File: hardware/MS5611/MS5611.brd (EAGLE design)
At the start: 15 x 16 mm, 4 parts, among them U1 MS5611, U2 EM406FLAT

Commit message: MS5611
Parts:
- C2: value 100nF -> 0.1uF
- moved R1 6.38 mm to (10.8, 9.47), turned to 270 degrees
- moved U1 0.46 mm to (7.57, 10.4)
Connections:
- removed net N$6: U1.4, U2.5
- new net N$3: U1.5
- new net VCC: U2.1
- net CSB: now also U1.4, U2.5; no longer U1.5
- net N$1: now also C2.1, U1.1; no longer R1.1, U2.2
- net N$2: now also R1.1, U1.6; no longer C2.1, U1.1, U2.1
- net SDO: now also U2.2; no longer U1.6
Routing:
- net N$2: track 11.5 -> 2.34 mm
- net SDO: track 15.1 -> 7.38 mm, vias 0 -> 2
- net CSB: track 0.00 -> 5.05 mm
- net N$6: track 4.81 -> 0.00 mm
- net SDI: track 12.8 -> 16.5 mm
- net SCK: track 16.1 -> 19.5 mm
- net GND: track 10.3 -> 8.08 mm, vias 1 -> 2
- removed copper zone on layer 1, net GND
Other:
- board size 15 x 16 mm -> 14.6 x 14.6 mm
- board text added: "ICARUS SENSORS MS5611 SPI board revA"
- board text removed: "ICARUS SENSORS MS5803 SPI board revA"

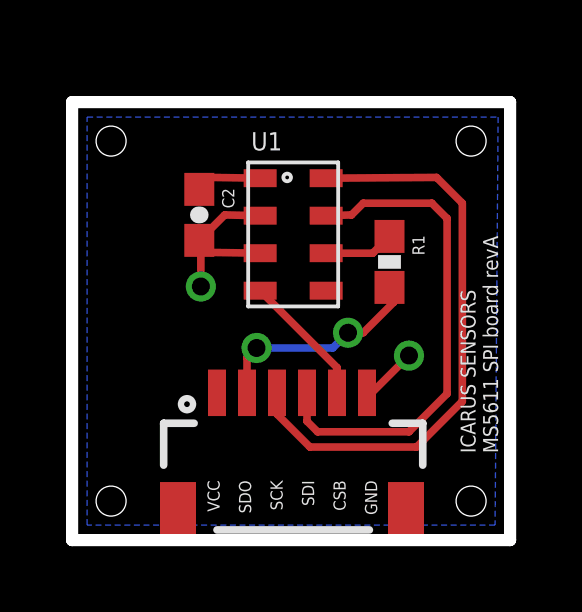
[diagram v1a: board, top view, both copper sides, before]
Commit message: borderless
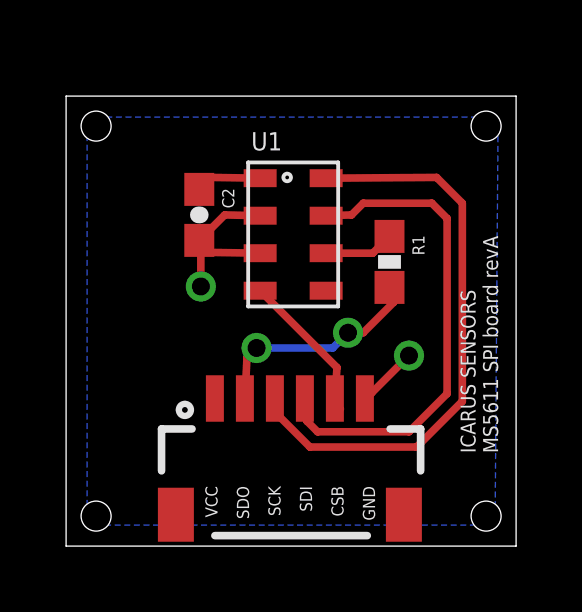
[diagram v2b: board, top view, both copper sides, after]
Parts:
- moved U2 0.20 mm to (7.50, 2.00)
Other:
- board size 14.6 x 14.6 mm -> 15 x 15 mm
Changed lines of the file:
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@@
 <setting verticaltext="up"/>
 </settings>
-<grid distance="0.01" unitdist="inch" unit="inch" style="lines" multiple="1" display="yes" altdistance="0.001" altunitdist="inch" altunit="inch"/>
+<grid distance="1" unitdist="mm" unit="mm" style="lines" multiple="1" display="yes" altdistance="0.001" altunitdist="inch" altunit="inch"/>
 <layers>
 <layer number="1" name="Top" color="4" fill="1" visible="yes" active="yes"/>
@@
 <board>
 <plain>
-<wire x1="0.2" y1="0.2" x2="0.2" y2="14.8" width="0.4064" layer="20"/>
-<wire x1="0.2" y1="14.8" x2="14.8" y2="14.8" width="0.4064" layer="20"/>
-<wire x1="14.8" y1="14.8" x2="14.8" y2="0.2" width="0.4064" layer="20"/>
-<wire x1="14.8" y1="0.2" x2="0.2" y2="0.2" width="0.4064" layer="20"/>
-<hole x="1.5" y="13.5" drill="1"/>
-<hole x="13.5" y="13.5" drill="1"/>
-<hole x="13.5" y="1.5" drill="1"/>
-<hole x="1.5" y="1.5" drill="1"/>
+<wire x1="0" y1="0" x2="0" y2="15" width="0" layer="20"/>
+<wire x1="0" y1="15" x2="15" y2="15" width="0" layer="20"/>
+<wire x1="15" y1="15" x2="15" y2="0" width="0" layer="20"/>
+<wire x1="15" y1="0" x2="0" y2="0" width="0" layer="20"/>
+<hole x="1" y="14" drill="1"/>
+<hole x="14" y="14" drill="1"/>
+<hole x="14" y="1" drill="1"/>
+<hole x="1" y="1" drill="1"/>
 <text x="14.4" y="3.1" size="0.5" layer="25" font="vector" ratio="9" rot="R90">ICARUS SENSORS
 MS5611 SPI board revA</text>
@@
 <attribute name="NAME" x="6.1692" y="13.1886" size="0.6096" layer="25"/>
 </element>
-<element name="U2" library="icarus_sensors" package="EM406-FLAT" value="EM406FLAT" x="7.57" y="2.19" smashed="yes"/>
+<element name="U2" library="icarus_sensors" package="EM406-FLAT" value="EM406FLAT" x="7.5" y="2" smashed="yes"/>
 <element name="C2" library="SparkFun-Capacitors" package="0603-CAP" value="0.1uF" x="4.44" y="11.04" smashed="yes" rot="R270">
 <attribute name="NAME" x="5.202" y="11.929" size="0.4064" layer="25" font="vector" rot="R270"/>
@@
 <contactref element="U1" pad="7"/>
 <contactref element="U2" pad="4"/>
-<wire x1="8.03" y1="5.11" x2="8.03" y2="4.162" width="0.254" layer="1"/>
+<wire x1="7.96" y1="4.92" x2="8.03" y2="4.162" width="0.254" layer="1"/>
 <wire x1="8.03" y1="4.162" x2="8.382" y2="3.81" width="0.254" layer="1"/>
 <wire x1="8.382" y1="3.81" x2="11.43" y2="3.81" width="0.254" layer="1"/>
@@
 <contactref element="U1" pad="8"/>
 <contactref element="U2" pad="3"/>
-<wire x1="7.03" y1="5.11" x2="7.03" y2="4.4" width="0.254" layer="1"/>
+<wire x1="6.96" y1="4.92" x2="7.03" y2="4.4" width="0.254" layer="1"/>
 <wire x1="7.03" y1="4.4" x2="8.128" y2="3.302" width="0.254" layer="1"/>
 <wire x1="8.128" y1="3.302" x2="11.684" y2="3.302" width="0.254" layer="1"/>
@@
 <wire x1="4.841" y1="9.789" x2="4.44" y2="10.19" width="0.254" layer="1"/>
 <via x="11.43" y="6.35" extent="1-16" drill="0.6"/>
-<wire x1="10.03" y1="5.11" x2="10.19" y2="5.11" width="0.254" layer="1"/>
+<wire x1="9.96" y1="4.92" x2="10.19" y2="5.11" width="0.254" layer="1"/>
 <wire x1="10.19" y1="5.11" x2="11.43" y2="6.35" width="0.254" layer="1"/>
 </signal>
@@
 <contactref element="U2" pad="5"/>
 <contactref element="U1" pad="4"/>
-<wire x1="9.03" y1="5.11" x2="9.03" y2="4.686" width="0.254" layer="1"/>
+<wire x1="8.96" y1="4.92" x2="9.03" y2="4.686" width="0.254" layer="1"/>
 <wire x1="9.03" y1="4.686" x2="9.144" y2="4.572" width="0.254" layer="1"/>
-<wire x1="9.03" y1="5.11" x2="9.03" y2="5.9528" width="0.254" layer="1"/>
+<wire x1="8.96" y1="4.92" x2="9.03" y2="5.9528" width="0.254" layer="1"/>
 <wire x1="9.03" y1="5.9528" x2="6.4692" y2="8.5136" width="0.254" layer="1"/>
 </signal>
@@
 <contactref element="R1" pad="2"/>
 <contactref element="U2" pad="2"/>
-<wire x1="6.03" y1="5.11" x2="6.03" y2="6.284" width="0.254" layer="1"/>
+<wire x1="5.96" y1="4.92" x2="6.03" y2="6.284" width="0.254" layer="1"/>
 <wire x1="6.03" y1="6.284" x2="6.35" y2="6.604" width="0.254" layer="1"/>
 <via x="6.35" y="6.604" extent="1-16" drill="0.6"/>

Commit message: initial shield
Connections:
- removed net N$1: C2.1, U1.1
- net VCC: now also C2.1, U1.1
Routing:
- net VCC: track 0.00 -> 10.9 mm
- net N$1: track 2.19 -> 0.00 mm
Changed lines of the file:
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@@
 <setting verticaltext="up"/>
 </settings>
-<grid distance="1" unitdist="mm" unit="mm" style="lines" multiple="1" display="yes" altdistance="0.001" altunitdist="inch" altunit="inch"/>
+<grid distance="10" unitdist="mil" unit="mil" style="lines" multiple="1" display="yes" altdistance="0.001" altunitdist="inch" altunit="inch"/>
 <layers>
 <layer number="1" name="Top" color="4" fill="1" visible="yes" active="yes"/>
@@
 <wire x1="9.03" y1="5.9528" x2="6.4692" y2="8.5136" width="0.254" layer="1"/>
 </signal>
-<signal name="N$1">
+<signal name="VCC">
+<contactref element="U2" pad="1"/>
 <contactref element="C2" pad="1"/>
 <contactref element="U1" pad="1"/>
-<wire x1="6.4692" y1="12.2636" x2="4.839" y2="12.289" width="0.254" layer="1"/>
-<wire x1="4.839" y1="12.289" x2="4.44" y2="11.89" width="0.254" layer="1"/>
-</signal>
-<signal name="VCC">
-<contactref element="U2" pad="1"/>
+<wire x1="6.4692" y1="12.2636" x2="4.44" y2="12.2636" width="0.254" layer="1"/>
+<wire x1="4.44" y1="12.2636" x2="4.44" y2="11.89" width="0.254" layer="1"/>
+<wire x1="4.44" y1="11.89" x2="3.762" y2="11.89" width="0.254" layer="1"/>
+<wire x1="3.762" y1="11.89" x2="3.302" y2="11.43" width="0.254" layer="1"/>
+<wire x1="3.302" y1="11.43" x2="3.302" y2="6.578" width="0.254" layer="1"/>
+<wire x1="3.302" y1="6.578" x2="4.96" y2="4.92" width="0.254" layer="1"/>
 </signal>
 <signal name="N$2">
